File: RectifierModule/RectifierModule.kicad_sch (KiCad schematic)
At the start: 20 parts, among them J1 TransformerIn, J2 Rectified Out, J3 AuxIn, J4 VA, J5 Extra, J5 FAN, P1 Conn_WallPlug, U1 LM7812_TO220

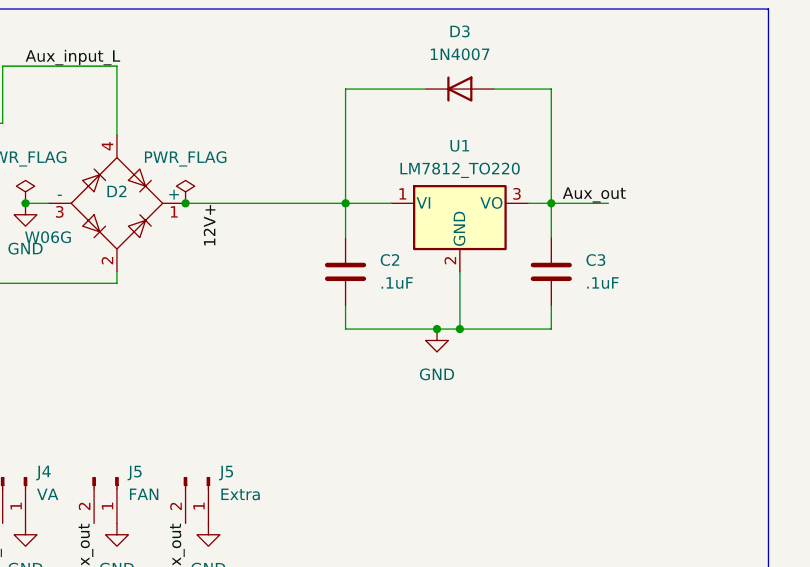
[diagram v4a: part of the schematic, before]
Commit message: Updated the capacitor at input of 7812
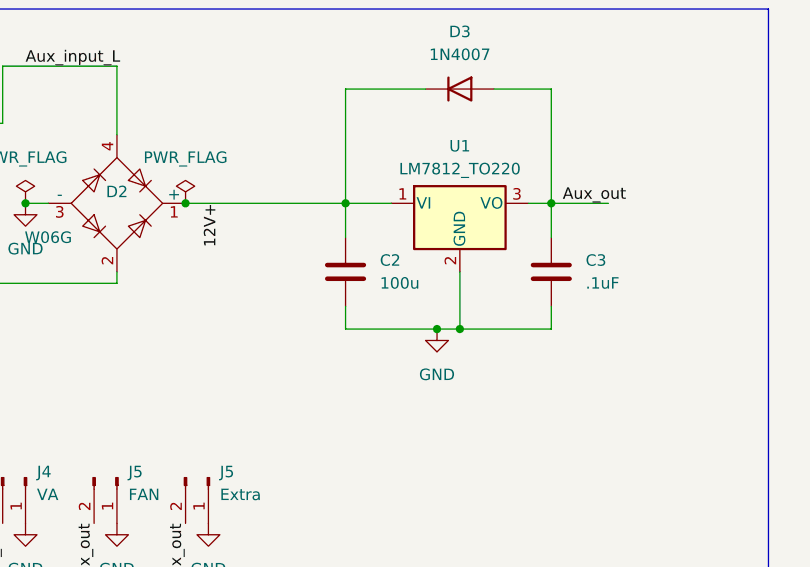
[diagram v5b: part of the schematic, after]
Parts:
- C2: value .1uF -> 100u; footprint Capacitor_THT:C_Disc_D4.3mm_W1.9mm_P5.00mm -> Capacitor_THT:C_Radial_D6.3mm_H11.0mm_P2.50mm
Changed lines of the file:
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@@
       (effects (font (size 1.27 1.27)) (justify left))
     )
-    (property "Value" ".1uF" (at 152.4 45.72 0)
+    (property "Value" "100u" (at 152.4 45.72 0)
       (effects (font (size 1.27 1.27)) (justify left))
     )
-    (property "Footprint" "Capacitor_THT:C_Disc_D4.3mm_W1.9mm_P5.00mm" (at 149.5552 48.26 0)
+    (property "Footprint" "Capacitor_THT:C_Radial_D6.3mm_H11.0mm_P2.50mm" (at 149.5552 48.26 0)
       (effects (font (size 1.27 1.27)) hide)
     )

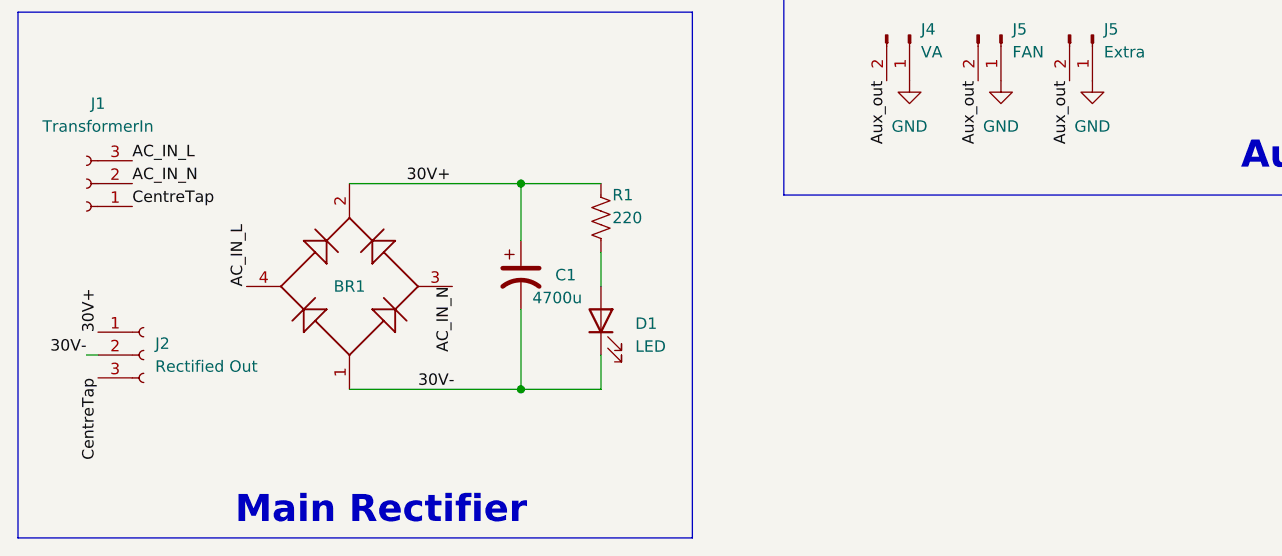
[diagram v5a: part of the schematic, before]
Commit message: Add mounting holes and their footprints
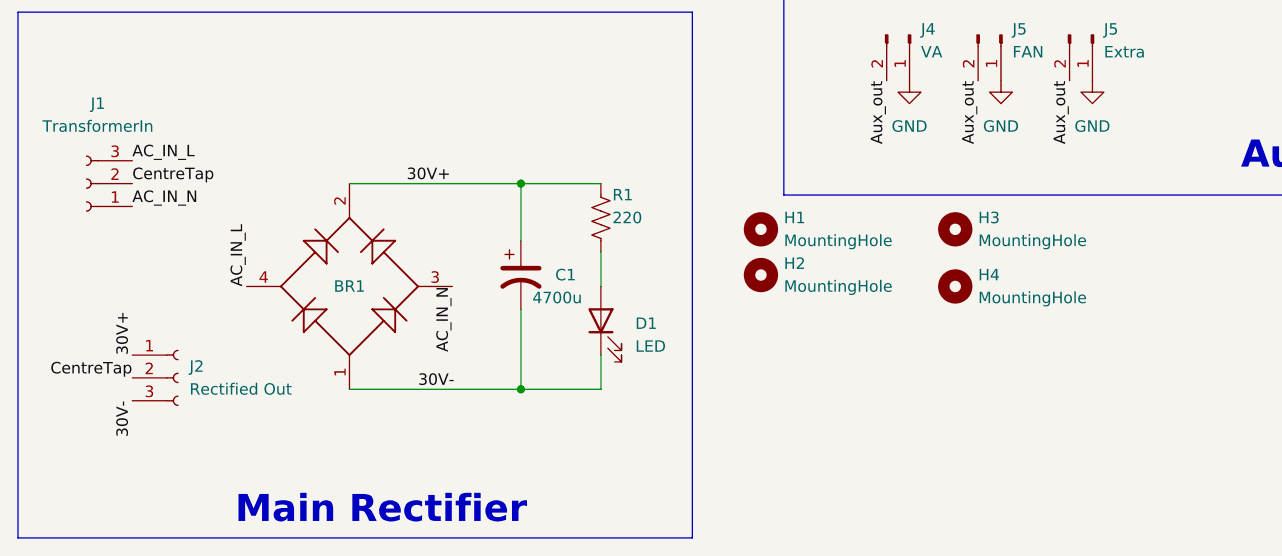
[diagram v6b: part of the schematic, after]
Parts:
- added H1, H2, H3, H4: MountingHole, MountingHole:MountingHole_2.5mm, symbol Mechanical:MountingHole
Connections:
- net 30V-: now also J2.3 (Pin_3); no longer J2.2 (Pin_2)
- net AC_IN_N: now also J1.1 (Pin_1); no longer J1.2 (Pin_2)
- net CentreTap: now also J1.2 (Pin_2), J2.2 (Pin_2); no longer J1.1 (Pin_1), J2.3 (Pin_3)
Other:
- moved on the sheet: J2
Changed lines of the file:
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@@
-    (stroke (width 0) (type default))
-  )
-  (wire (pts (xy 21.59 102.87) (xy 22.86 102.87))
     (stroke (width 0) (type default))
   )
@@
     (effects (font (size 1.27 1.27)) (justify right bottom))
   )
-  (label "30V+" (at 22.86 100.33 90) (fields_autoplaced)
-    (effects (font (size 1.27 1.27)) (justify left bottom))
+  (label "30V+" (at 26.67 102.87 90) (fields_autoplaced)
+    (effects (font (size 1.27 1.27)) (justify left bottom))
+  )
+  (label "30V-" (at 26.67 107.95 270) (fields_autoplaced)
+    (effects (font (size 1.27 1.27)) (justify right bottom))
   )
   (label "AC_IN_L" (at 39.37 95.25 90) (fields_autoplaced)
     (effects (font (size 1.27 1.27)) (justify left bottom))
-  )
-  (label "CentreTap" (at 26.67 86.36 0) (fields_autoplaced)
-    (effects (font (size 1.27 1.27)) (justify left bottom))
-  )
-  (label "CentreTap" (at 22.86 105.41 270) (fields_autoplaced)
-    (effects (font (size 1.27 1.27)) (justify right bottom))
   )
   (label "Aux_out" (at 120.65 72.39 270) (fields_autoplaced)
@@
     (effects (font (size 1.27 1.27)) (justify left bottom))
   )
+  (label "CentreTap" (at 26.67 83.82 0) (fields_autoplaced)
+    (effects (font (size 1.27 1.27)) (justify left bottom))
+  )
   (label "Aux_out" (at 172.72 36.83 0) (fields_autoplaced)
     (effects (font (size 1.27 1.27)) (justify left bottom))
   )
-  (label "AC_IN_N" (at 26.67 83.82 0) (fields_autoplaced)
-    (effects (font (size 1.27 1.27)) (justify left bottom))
-  )
   (label "CentreTap" (at 62.23 27.94 0) (fields_autoplaced)
     (effects (font (size 1.27 1.27)) (justify left bottom))
+  )
+  (label "CentreTap" (at 26.67 105.41 180) (fields_autoplaced)
+    (effects (font (size 1.27 1.27)) (justify right bottom))
   )
   (label "Aux_out" (at 110.49 72.39 270) (fields_autoplaced)
@@
     (effects (font (size 1.27 1.27)) (justify right bottom))
   )
-  (label "30V-" (at 21.59 102.87 180) (fields_autoplaced)
-    (effects (font (size 1.27 1.27)) (justify right bottom))
+  (label "AC_IN_N" (at 26.67 86.36 0) (fields_autoplaced)
+    (effects (font (size 1.27 1.27)) (justify left bottom))
   )
   (label "30V-" (at 58.42 106.68 0) (fields_autoplaced)
@@
   (symbol (lib_id "power:GND") (at 123.19 72.39 0) (unit 1)
     (in_bom yes) (on_board yes) (dnp no) (fields_autoplaced)
-    (property "Reference" "#PWR04" (at 123.19 78.74 0)
+    (property "Reference" "#PWR03" (at 123.19 78.74 0)
       (effects (font (size 1.27 1.27)) hide)
     )
@@
       (project "RectifierModule"
         (path "/85225bbb-a12f-4483-ac90-767368bd8ae2"
-          (reference "#PWR04") (unit 1)
+          (reference "#PWR03") (unit 1)
         )
       )
@@
   (symbol (lib_id "power:GND") (at 113.03 72.39 0) (unit 1)
     (in_bom yes) (on_board yes) (dnp no) (fields_autoplaced)
-    (property "Reference" "#PWR03" (at 113.03 78.74 0)
+    (property "Reference" "#PWR02" (at 113.03 78.74 0)
       (effects (font (size 1.27 1.27)) hide)
     )
@@
       (project "RectifierModule"
         (path "/85225bbb-a12f-4483-ac90-767368bd8ae2"
-          (reference "#PWR03") (unit 1)
+          (reference "#PWR02") (unit 1)
+        )
+      )
+    )
+  )
+  (symbol (lib_id "Mechanical:MountingHole") (at 96.52 88.9 0) (unit 1)
+    (in_bom yes) (on_board yes) (dnp no) (fields_autoplaced)
+    (property "Reference" "H1" (at 99.06 87.63 0)
+      (effects (font (size 1.27 1.27)) (justify left))
+    )
+    (property "Value" "MountingHole" (at 99.06 90.17 0)
+      (effects (font (size 1.27 1.27)) (justify left))
+    )
+    (property "Footprint" "MountingHole:MountingHole_2.5mm" (at 96.52 88.9 0)
+      (effects (font (size 1.27 1.27)) hide)
+    )
+    (property "Datasheet" "~" (at 96.52 88.9 0)
+      (effects (font (size 1.27 1.27)) hide)
+    )
+    (instances
+      (project "RectifierModule"
+        (path "/85225bbb-a12f-4483-ac90-767368bd8ae2"
+          (reference "H1") (unit 1)
         )
       )
@@
       (effects (font (size 1.27 1.27)))
     )
-    (property "Footprint" "Connector_JST:JST_VH_B3P-VH-B_1x03_P3.96mm_Vertical" (at 21.59 83.82 0)
+    (property "Footprint" "Connector_JST:JST_VH_B3P-VH-B_1x03_P3.96mm_Vertical" (at 22.86 88.9 0)
       (effects (font (size 1.27 1.27)) hide)
     )
@@
     )
   )
-  (symbol (lib_id "Connector:Conn_01x03_Socket") (at 27.94 102.87 0) (unit 1)
-    (in_bom yes) (on_board yes) (dnp no) (fields_autoplaced)
-    (property "Reference" "J2" (at 29.21 101.6 0)
-      (effects (font (size 1.27 1.27)) (justify left))
-    )
-    (property "Value" "Rectified Out" (at 29.21 104.14 0)
-      (effects (font (size 1.27 1.27)) (justify left))
-    )
-    (property "Footprint" "Connector_JST:JST_VH_B3P-VH-B_1x03_P3.96mm_Vertical" (at 27.94 102.87 0)
-      (effects (font (size 1.27 1.27)) hide)
-    )
-    (property "Datasheet" "~" (at 27.94 102.87 0)
+  (symbol (lib_id "Connector:Conn_01x03_Socket") (at 31.75 105.41 0) (unit 1)
+    (in_bom yes) (on_board yes) (dnp no) (fields_autoplaced)
+    (property "Reference" "J2" (at 33.02 104.14 0)
+      (effects (font (size 1.27 1.27)) (justify left))
+    )
+    (property "Value" "Rectified Out" (at 33.02 106.68 0)
+      (effects (font (size 1.27 1.27)) (justify left))
+    )
+    (property "Footprint" "Connector_JST:JST_VH_B3P-VH-B_1x03_P3.96mm_Vertical" (at 31.75 105.41 0)
+      (effects (font (size 1.27 1.27)) hide)
+    )
+    (property "Datasheet" "~" (at 31.75 105.41 0)
       (effects (font (size 1.27 1.27)) hide)
     )
@@
         (path "/85225bbb-a12f-4483-ac90-767368bd8ae2"
           (reference "J2") (unit 1)
+        )
+      )
+    )
+  )
+  (symbol (lib_id "Mechanical:MountingHole") (at 118.11 95.25 0) (unit 1)
+    (in_bom yes) (on_board yes) (dnp no) (fields_autoplaced)
+    (property "Reference" "H4" (at 120.65 93.98 0)
+      (effects (font (size 1.27 1.27)) (justify left))
+    )
+    (property "Value" "MountingHole" (at 120.65 96.52 0)
+      (effects (font (size 1.27 1.27)) (justify left))
+    )
+    (property "Footprint" "MountingHole:MountingHole_2.5mm" (at 118.11 95.25 0)
+      (effects (font (size 1.27 1.27)) hide)
+    )
+    (property "Datasheet" "~" (at 118.11 95.25 0)
+      (effects (font (size 1.27 1.27)) hide)
+    )
+    (instances
+      (project "RectifierModule"
+        (path "/85225bbb-a12f-4483-ac90-767368bd8ae2"
+          (reference "H4") (unit 1)
         )
       )
@@
   (symbol (lib_id "power:GND") (at 133.35 72.39 0) (unit 1)
     (in_bom yes) (on_board yes) (dnp no) (fields_autoplaced)
-    (property "Reference" "#PWR05" (at 133.35 78.74 0)
+    (property "Reference" "#PWR04" (at 133.35 78.74 0)
       (effects (font (size 1.27 1.27)) hide)
     )
@@
       (project "RectifierModule"
         (path "/85225bbb-a12f-4483-ac90-767368bd8ae2"
-          (reference "#PWR05") (unit 1)
+          (reference "#PWR04") (unit 1)
         )
       )
@@
         (path "/85225bbb-a12f-4483-ac90-767368bd8ae2"
           (reference "#FLG01") (unit 1)
+        )
+      )
+    )
+  )
+  (symbol (lib_id "Mechanical:MountingHole") (at 96.52 93.98 0) (unit 1)
+    (in_bom yes) (on_board yes) (dnp no) (fields_autoplaced)
+    (property "Reference" "H2" (at 99.06 92.71 0)
+      (effects (font (size 1.27 1.27)) (justify left))
+    )
+    (property "Value" "MountingHole" (at 99.06 95.25 0)
+      (effects (font (size 1.27 1.27)) (justify left))
+    )
+    (property "Footprint" "MountingHole:MountingHole_2.5mm" (at 96.52 93.98 0)
+      (effects (font (size 1.27 1.27)) hide)
+    )
+    (property "Datasheet" "~" (at 96.52 93.98 0)
+      (effects (font (size 1.27 1.27)) hide)
+    )
+    (instances
+      (project "RectifierModule"
+        (path "/85225bbb-a12f-4483-ac90-767368bd8ae2"
+          (reference "H2") (unit 1)
         )
       )
@@
     )
   )
+  (symbol (lib_id "Mechanical:MountingHole") (at 118.11 88.9 0) (unit 1)
+    (in_bom yes) (on_board yes) (dnp no) (fields_autoplaced)
+    (property "Reference" "H3" (at 120.65 87.63 0)
+      (effects (font (size 1.27 1.27)) (justify left))
+    )
+    (property "Value" "MountingHole" (at 120.65 90.17 0)
+      (effects (font (size 1.27 1.27)) (justify left))
+    )
+    (property "Footprint" "MountingHole:MountingHole_2.5mm" (at 118.11 88.9 0)
+      (effects (font (size 1.27 1.27)) hide)
+    )
+    (property "Datasheet" "~" (at 118.11 88.9 0)
+      (effects (font (size 1.27 1.27)) hide)
+    )
+    (instances
+      (project "RectifierModule"
+        (path "/85225bbb-a12f-4483-ac90-767368bd8ae2"
+          (reference "H3") (unit 1)
+        )
+      )
+    )
+  )
   (symbol (lib_id "power:GND") (at 158.75 50.8 0) (unit 1)
     (in_bom yes) (on_board yes) (dnp no) (fields_autoplaced)
-    (property "Reference" "#PWR02" (at 158.75 57.15 0)
+    (property "Reference" "#PWR05" (at 158.75 57.15 0)
       (effects (font (size 1.27 1.27)) hide)
     )
@@
       (project "RectifierModule"
         (path "/85225bbb-a12f-4483-ac90-767368bd8ae2"
-          (reference "#PWR02") (unit 1)
-        )
-      )
+          (reference "#PWR05") (unit 1)
+        )
+      )

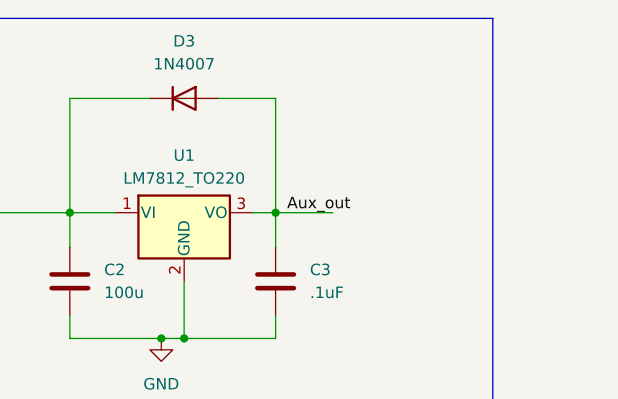
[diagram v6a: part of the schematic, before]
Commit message: Added heat sink and made changes to accommodate the heatsink
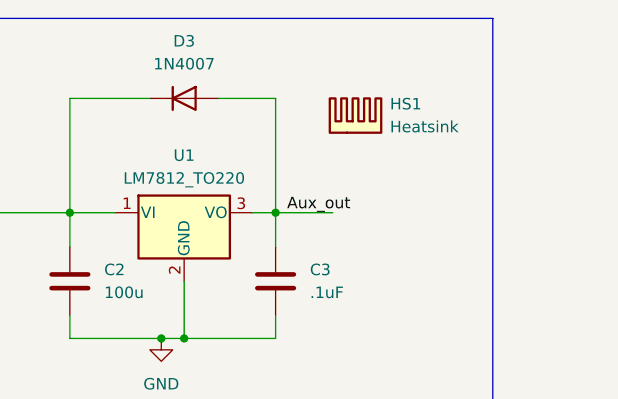
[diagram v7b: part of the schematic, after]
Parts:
- added HS1: Heatsink, Heatsink:Heatsink_Stonecold_HS-S03_13.21x12.7mm, symbol Mechanical:Heatsink
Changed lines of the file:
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@@
+    )
+  )
+  (symbol (lib_id "Mechanical:Heatsink") (at 180.34 27.94 0) (unit 1)
+    (in_bom yes) (on_board yes) (dnp no) (fields_autoplaced)
+    (property "Reference" "HS1" (at 184.15 24.765 0)
+      (effects (font (size 1.27 1.27)) (justify left))
+    )
+    (property "Value" "Heatsink" (at 184.15 27.305 0)
+      (effects (font (size 1.27 1.27)) (justify left))
+    )
+    (property "Footprint" "Heatsink:Heatsink_Stonecold_HS-S03_13.21x12.7mm" (at 180.6448 27.94 0)
+      (effects (font (size 1.27 1.27)) hide)
+    )
+    (property "Datasheet" "~" (at 180.6448 27.94 0)
+      (effects (font (size 1.27 1.27)) hide)
+    )
+    (instances
+      (project "RectifierModule"
+        (path "/85225bbb-a12f-4483-ac90-767368bd8ae2"
+          (reference "HS1") (unit 1)
+        )
+      )
     )
   )
